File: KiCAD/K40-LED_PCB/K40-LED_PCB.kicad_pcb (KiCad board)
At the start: 2 copper layers, 111.8 x 58.4 mm, 10 parts, among them J1 1776275-2, U1 LDD_350HS

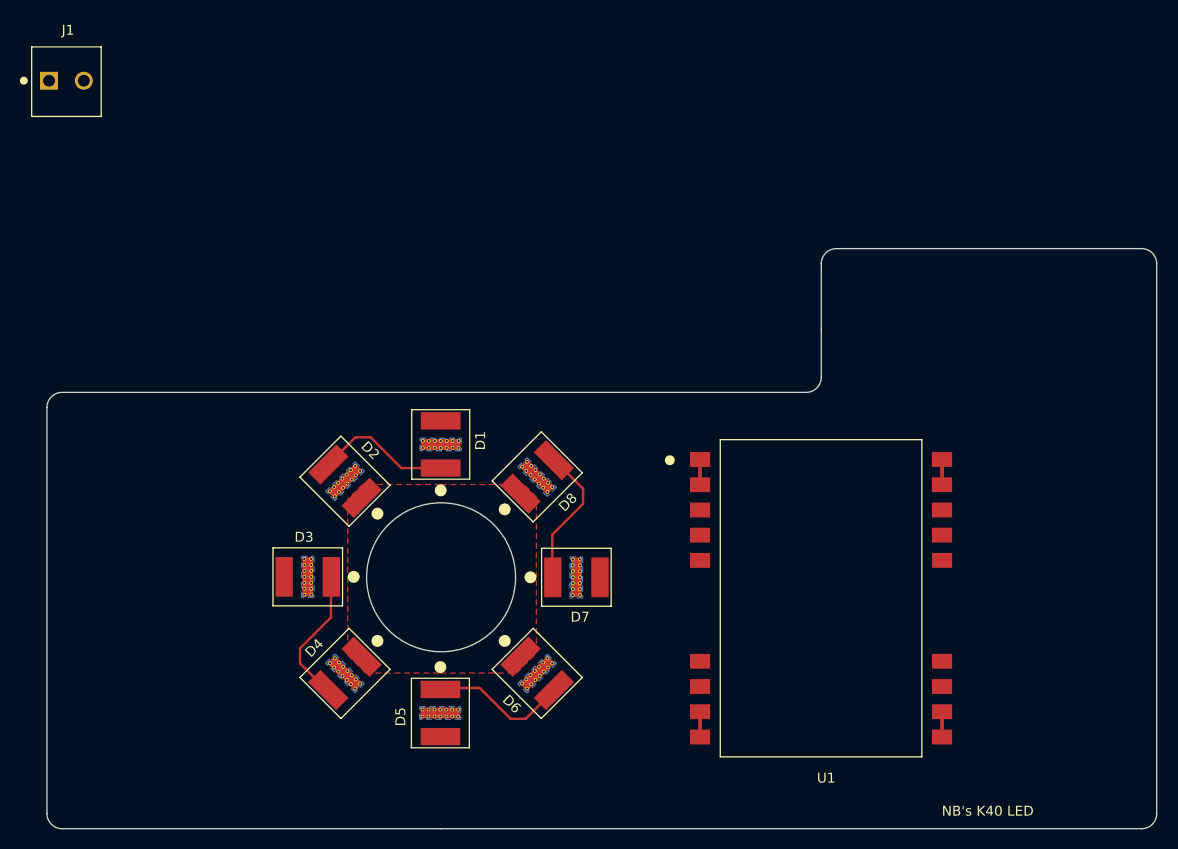
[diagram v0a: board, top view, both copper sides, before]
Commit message: SPST switch footprint completed & finished routing
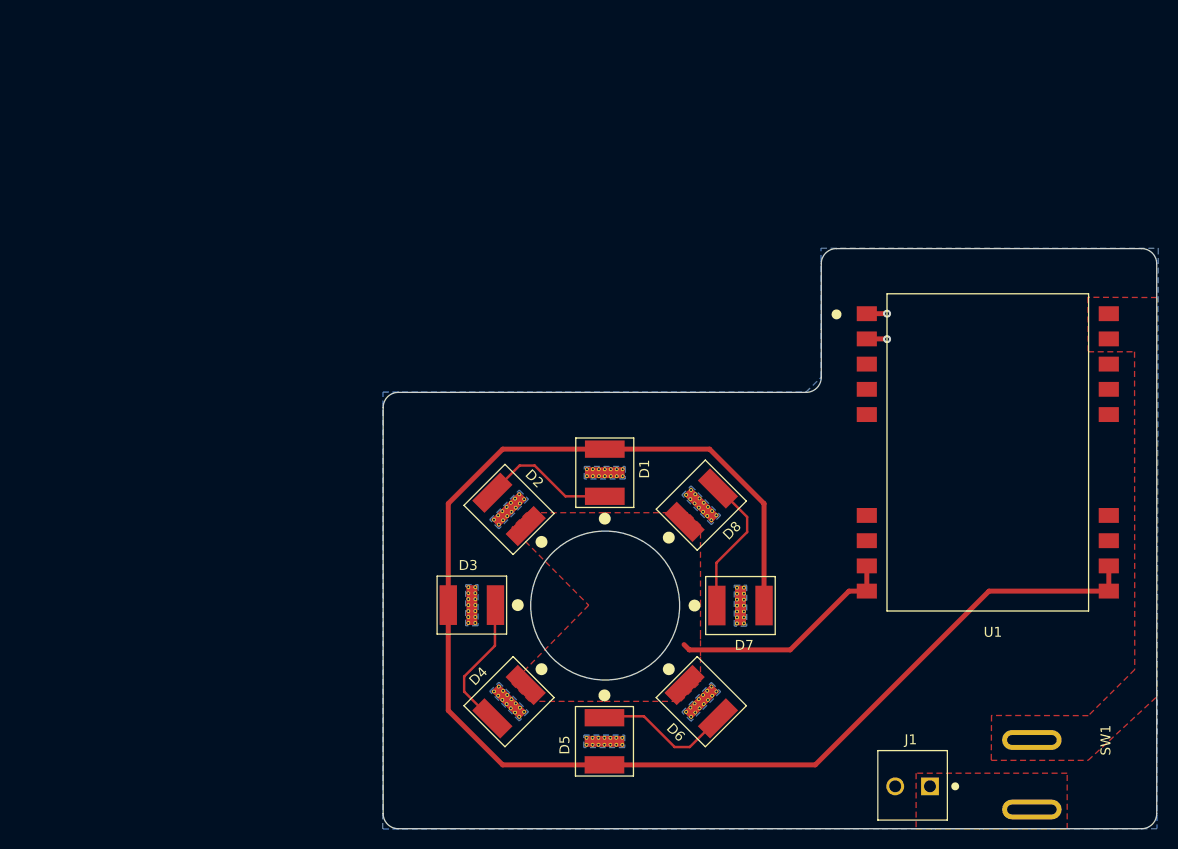
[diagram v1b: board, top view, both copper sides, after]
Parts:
- added SW1: SW_SPST, RA1113112R:RA1113112R, F.Cu at (150.5, 138.4)
- moved J1 113.7 mm to (140.2, 143.1), turned to 180 degrees
- moved U1 22.3 mm to (133.9, 91.0)
- moved D1 16.8 mm to (112.5, 109.1)
- moved D2 16.8 mm to (99.7, 110.0)
- moved D3 16.8 mm to (91.7, 119.8)
- moved D4 16.8 mm to (92.6, 132.7)
- moved D5 16.8 mm to (102.5, 140.9)
- moved D6 16.8 mm to (115.3, 139.7)
- moved D7 16.8 mm to (123.5, 129.8)
- moved D8 16.8 mm to (122.4, 116.6)
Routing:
- net +Led: track 2.54 -> 146.0 mm
- net -Led: track 2.54 -> 23.6 mm
- net VIn: track 2.58 -> 0.00 mm
- net VOut: track 2.54 -> 4.10 mm, vias 0 -> 2
- added copper zone on F.Cu, net VIn
- added copper zone on B.Cu, net VOut
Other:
- board size 111.8 x 58.4 mm -> 77.9 x 58.4 mm
- board text removed: "NB's K40 LED"
